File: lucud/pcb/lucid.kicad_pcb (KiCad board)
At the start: 4 copper layers, 50.8 x 83.8 mm, 13 parts, among them J1 Conn_02x05_Odd_Even, J2 Conn_02x30_Odd_Even, U1 STM32F373VCTx, U2 R-78E3.3-0.5

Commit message: Worked on the PCB
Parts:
- added C10: 1uF 25V, Capacitor_SMD:C_0603_1608Metric, F.Cu at (167.6, 92.7)
- added C11: 1uF 6.3V, Capacitor_SMD:C_0603_1608Metric, F.Cu at (162.6, 92.7)
- added C12: 1uF 6.3V, Capacitor_SMD:C_0603_1608Metric, F.Cu at (184.8, 84.3)
- added C13: 1uF 6.3V, Capacitor_SMD:C_0603_1608Metric, F.Cu at (184.8, 82.8)
- added U5: R-78E5.0-0.5, Converter_DCDC:Converter_DCDC_RECOM_R-78E-0.5_THT, F.Cu at (167.6, 96.5)
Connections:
- net Net-(J2-Pad10) renamed /I.1
- net Net-(J2-Pad11) renamed /O.2
- net Net-(J2-Pad12) renamed /I.2
- net Net-(J2-Pad13) renamed /O.3
- net Net-(J2-Pad14) renamed /I.3
- net Net-(J2-Pad15) renamed /O.4
- net Net-(J2-Pad16) renamed /I.4
- net Net-(J2-Pad17) renamed /O.5
- net Net-(J2-Pad18) renamed /I.5
- net Net-(J2-Pad19) renamed /O.6
- net Net-(J2-Pad20) renamed /I.6
- net Net-(J2-Pad21) renamed /O.7
- net Net-(J2-Pad22) renamed /I.7
- net Net-(J2-Pad23) renamed /O.8
- net Net-(J2-Pad24) renamed /I.8
- net Net-(J2-Pad25) renamed /0.9
- net Net-(J2-Pad26) renamed /I.9
- net Net-(J2-Pad27) renamed /O.10
- net Net-(J2-Pad28) renamed /I.10
- net Net-(J2-Pad29) renamed /O.11
- net Net-(J2-Pad30) renamed /I.11
- net Net-(J2-Pad31) renamed /O.12
- net Net-(J2-Pad32) renamed /I.12
- net Net-(J2-Pad33) renamed /O.13
- net Net-(J2-Pad34) renamed /I.13
- net Net-(J2-Pad35) renamed /O.14
- net Net-(J2-Pad36) renamed /I.14
- net Net-(J2-Pad37) renamed /O.15
- net Net-(J2-Pad38) renamed /I.15
- net Net-(J2-Pad7) renamed /O.0
- net Net-(J2-Pad8) renamed /I.0
- net Net-(J2-Pad9) renamed /O.1

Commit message: Routed some of the lines in.
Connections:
- net Net-(J2-Pad39) renamed /D0
- net Net-(J2-Pad40) renamed /B0
- net Net-(J2-Pad41) renamed /D1
- net Net-(J2-Pad42) renamed /B1
- net Net-(J2-Pad43) renamed /D2
- net Net-(J2-Pad44) renamed /B2
- net Net-(J2-Pad45) renamed /D3
- net Net-(J2-Pad46) renamed /B3
- net Net-(J2-Pad47) renamed /D4
- net Net-(J2-Pad49) renamed /D5
- net Net-(J2-Pad50) renamed /BOOT_PB
- net Net-(J2-Pad51) renamed /D6
- net Net-(J2-Pad52) renamed /USB_D-
- net Net-(J2-Pad53) renamed /D7
- net Net-(J2-Pad54) renamed /USB_D+
- net Net-(J2-Pad56) renamed /SWD_DAT
- net Net-(J2-Pad60) renamed /nRST
- J2 pad 58: Net-(J2-Pad58) -> /SWD_CLK
- U1 pad 72: Net-(U1-Pad72) -> /SWD_CLK

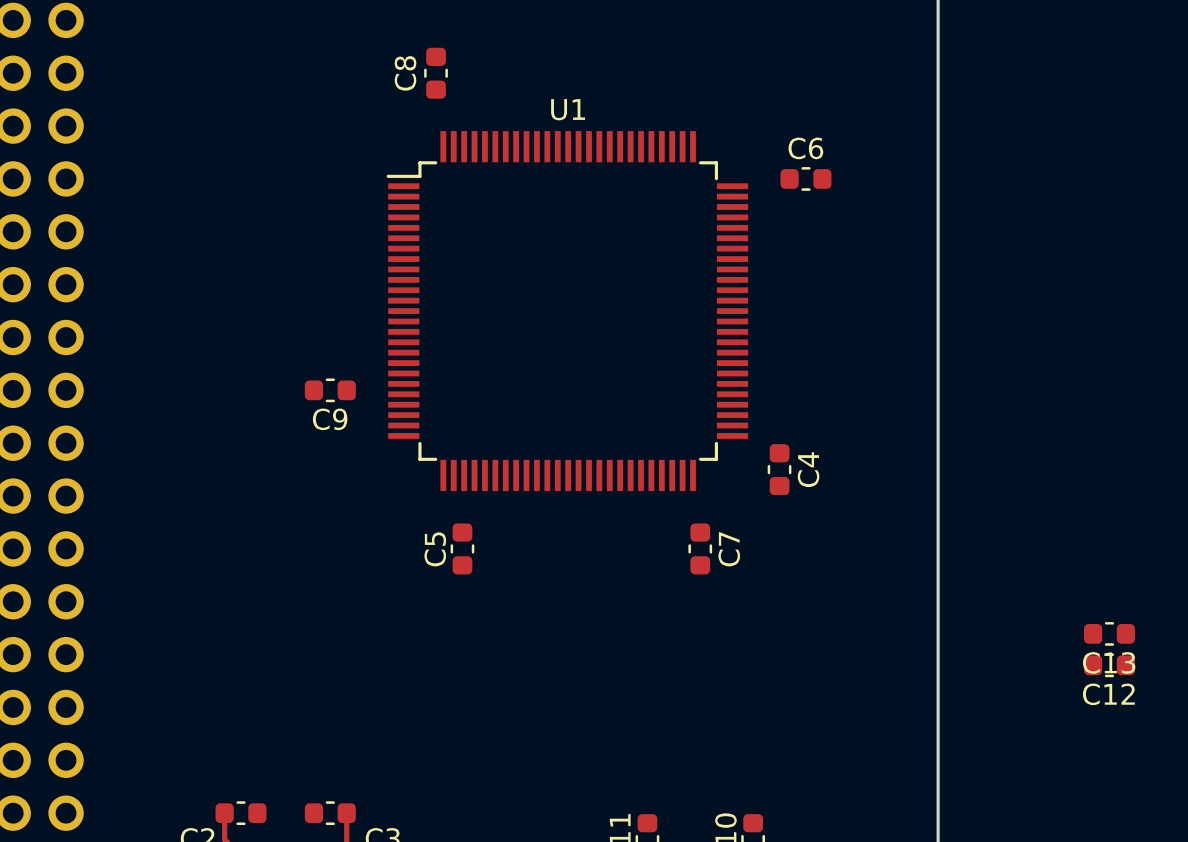
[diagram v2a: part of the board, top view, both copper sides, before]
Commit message: Added buffer parts
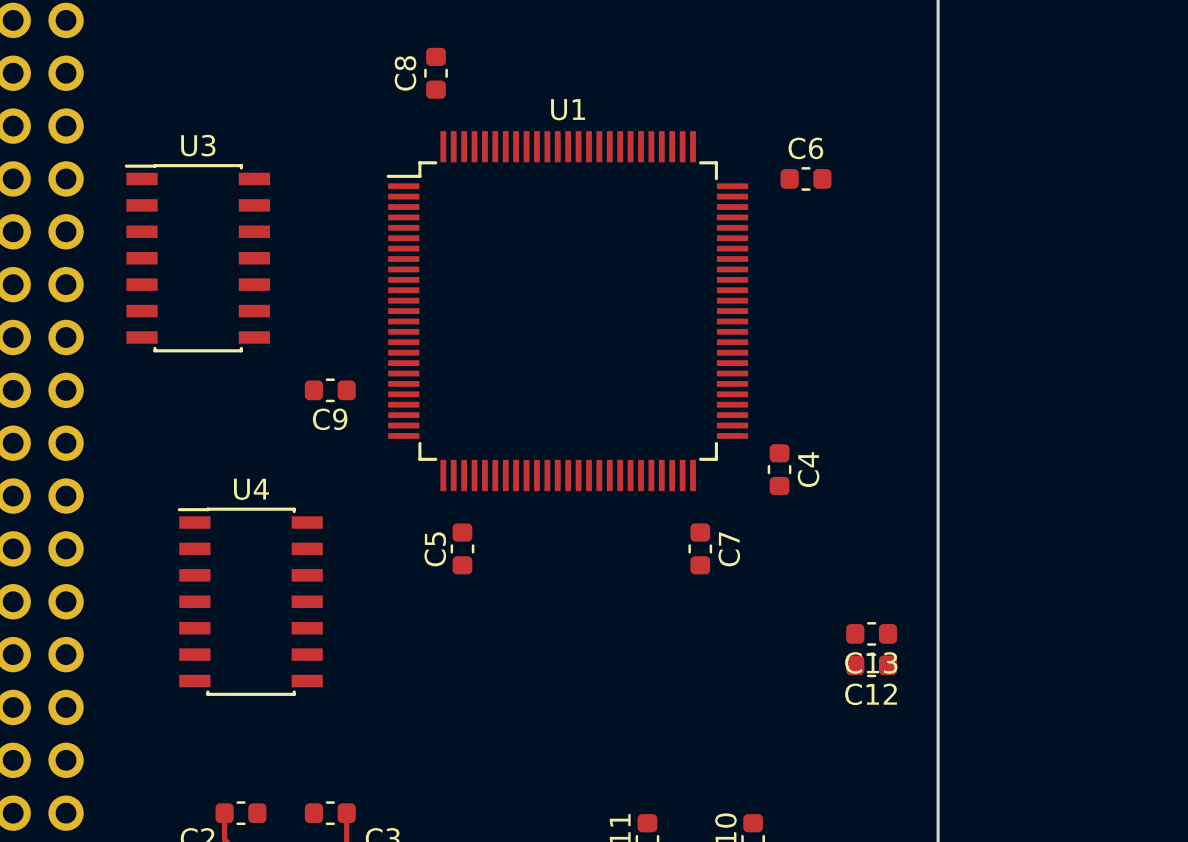
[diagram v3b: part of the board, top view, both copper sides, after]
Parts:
- added U3: 74LVC125, Package_SO:SOIC-14_3.9x8.7mm_P1.27mm, F.Cu at (141.0, 64.8)
- added U4: 74LVC125, Package_SO:SOIC-14_3.9x8.7mm_P1.27mm, F.Cu at (143.5, 81.3)
- moved C12 11.4 mm to (173.3, 84.3)
- moved C13 11.4 mm to (173.3, 82.8)
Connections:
- net Net-(U1-Pad23) renamed /MCU/AI.0
- net Net-(U1-Pad24) renamed /MCU/AI.1
- net Net-(U1-Pad25) renamed /MCU/AI.2
- net Net-(U1-Pad26) renamed /MCU/AI.3
- net Net-(U1-Pad29) renamed /MCU/AI.4
- net Net-(U1-Pad30) renamed /MCU/AI.5
- net Net-(U1-Pad31) renamed /MCU/AI.6
- net Net-(U1-Pad32) renamed /MCU/AI.7
- U1 pad 14: Net-(U1-Pad14) -> /nRST
- U1 pad 76: Net-(U1-Pad76) -> /SWD_DAT
